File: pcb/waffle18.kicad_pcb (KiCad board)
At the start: 2 copper layers, 39 parts, among them U1 XIAO-RP2350

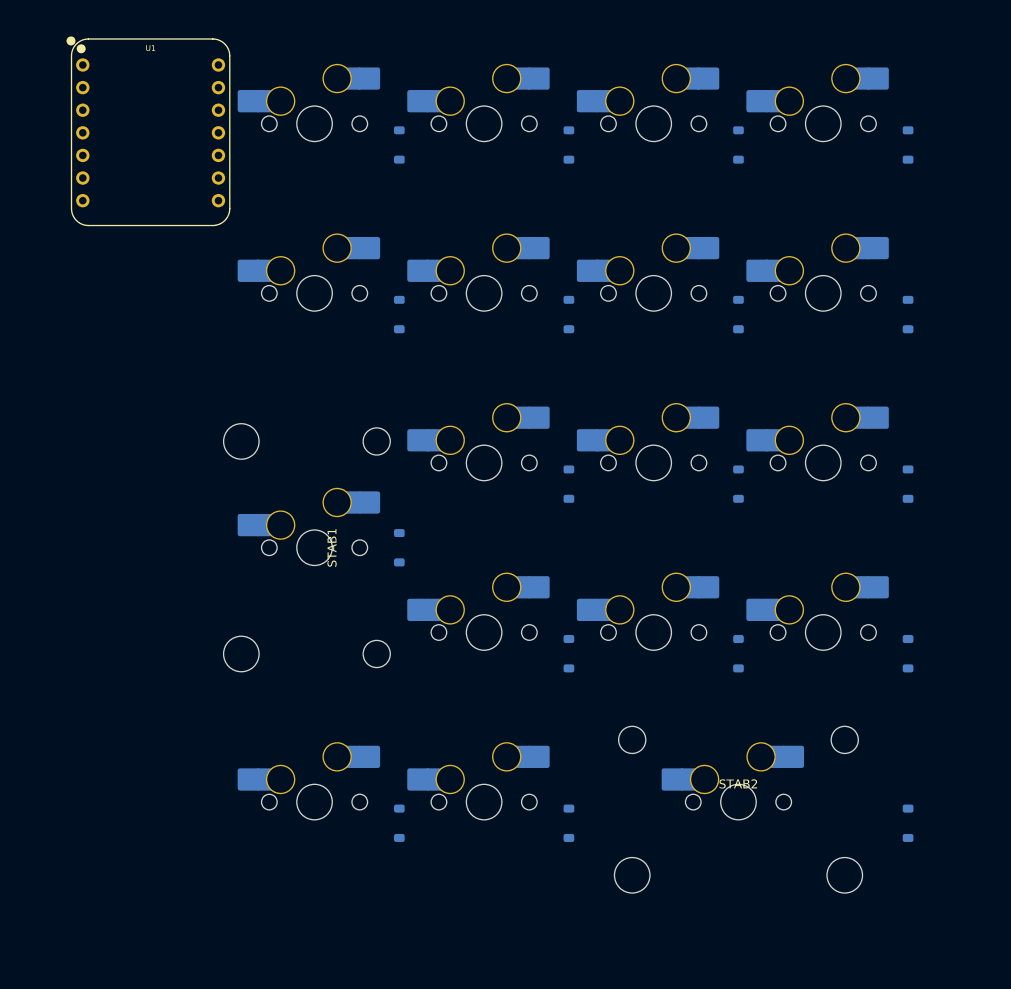
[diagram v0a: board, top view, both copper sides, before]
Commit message: feat(pcb): route tracks and place vias
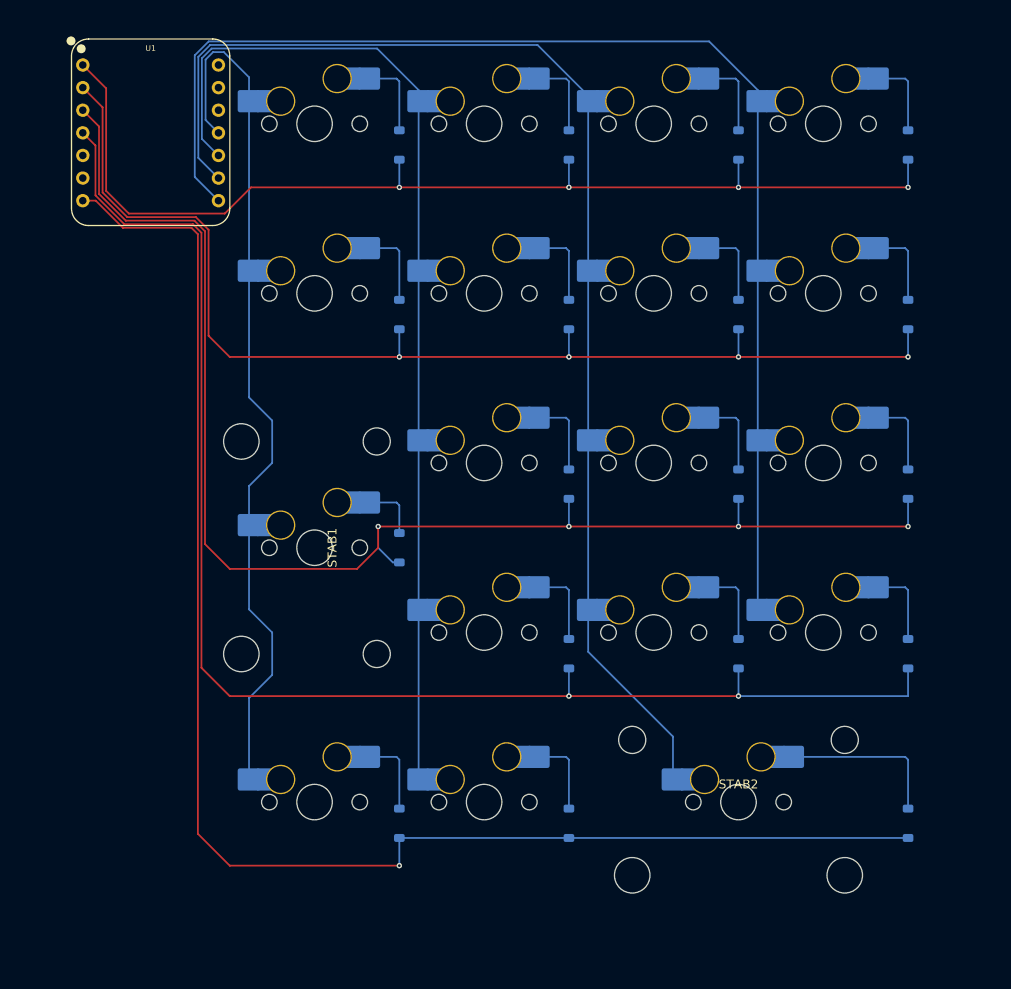
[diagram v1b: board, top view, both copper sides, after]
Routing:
- net /Row 4: track 0.00 -> 166.5 mm, vias 0 -> 1
- net /Row 3: track 0.00 -> 160.2 mm, vias 0 -> 2
- net /Row 2: track 0.00 -> 157.2 mm, vias 0 -> 4
- net /Column 2: track 0.00 -> 142.0 mm
- net /Column 3: track 0.00 -> 142.0 mm
- net /Row 1: track 0.00 -> 130.3 mm, vias 0 -> 4
- net /Row 0: track 0.00 -> 120.0 mm, vias 0 -> 4
- net /Column 1: track 0.00 -> 115.9 mm
- net /Column 0: track 0.00 -> 98.4 mm
- net Net-(D18-A): track 0.00 -> 18.6 mm
- net Net-(D8-A): track 0.00 -> 9.06 mm
- net Net-(D6-A): track 0.00 -> 9.06 mm
- net Net-(D17-A): track 0.00 -> 9.06 mm
- net Net-(D15-A): track 0.00 -> 9.06 mm
- net Net-(D13-A): track 0.00 -> 9.06 mm
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
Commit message: feat(pcb): add edge cuts
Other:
- board outline added: 102.6 x 99.9 mm
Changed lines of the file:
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@@
 		(tags "Cherry MX Keyboard Stabilizer 2.00u 2.25u 2.50u 2.75u Cutout")
 		(property "Reference" "STAB2"
-			(at 0 -2 0)
+			(at 0 9.525 0)
 			(layer "F.SilkS")
 			(effects
@@
 		(tags "Cherry MX Keyboard Stabilizer 2.00u 2.25u 2.50u 2.75u Cutout")
 		(property "Reference" "STAB1"
-			(at 0 -2 90)
+			(at 0 9.525 270)
 			(layer "F.SilkS")
 			(effects
@@
 		(at 96.181074 63.170756 90)
 		(property "Reference" "U1"
-			(at 9.5 0 0)
+			(at 0 -10 90)
 			(unlocked yes)
 			(layer "F.SilkS")
 			(effects
 				(font
-					(size 0.635 0.635)
-					(thickness 0.1016)
+					(size 1 1)
+					(thickness 0.15)
 				)
 			)
@@
 			)
 		)
-		(property "Description" "XIAO-RP2350-SMD by Seeed-Studio/OPL_Kicad_Library on GitHub, used under CC-BY-SA-4.0 / Modified field values"
+		(property "Description" "XIAO-Add-On by Seeed-Studio/OPL_Kicad_Library on GitHub, used under CC-BY-SA-4.0 / Removed unused holes and solderpaste margin overrides"
 			(at 0 0 90)
 			(unlocked yes)
@@
 		(sheetname "/")
 		(sheetfile "waffle18.kicad_sch")
-		(units
-			(unit
-				(name "A")
-				(pins "1" "2" "3" "4" "5" "6" "7" "8" "9" "10" "11" "12" "13" "14" "29"
-					"30" "28" "27" "26" "25" "24" "23" "22" "21" "20" "19" "18" "17" "16"
-					"15"
-				)
-			)
-		)
 		(attr through_hole)
 		(net_tie_pad_groups "1" "2" "3" "4" "5" "6" "7" "8" "9" "10" "11" "12"
@@
 		)
 	)
+	(gr_rect
+		(start 82.291074 51.629756)
+		(end 184.889824 151.498506)
+		(radius 5)
+		(stroke
+			(width 0.05)
+			(type solid)
+		)
+		(fill no)
+		(layer "Edge.Cuts")
+	)
 	(segment

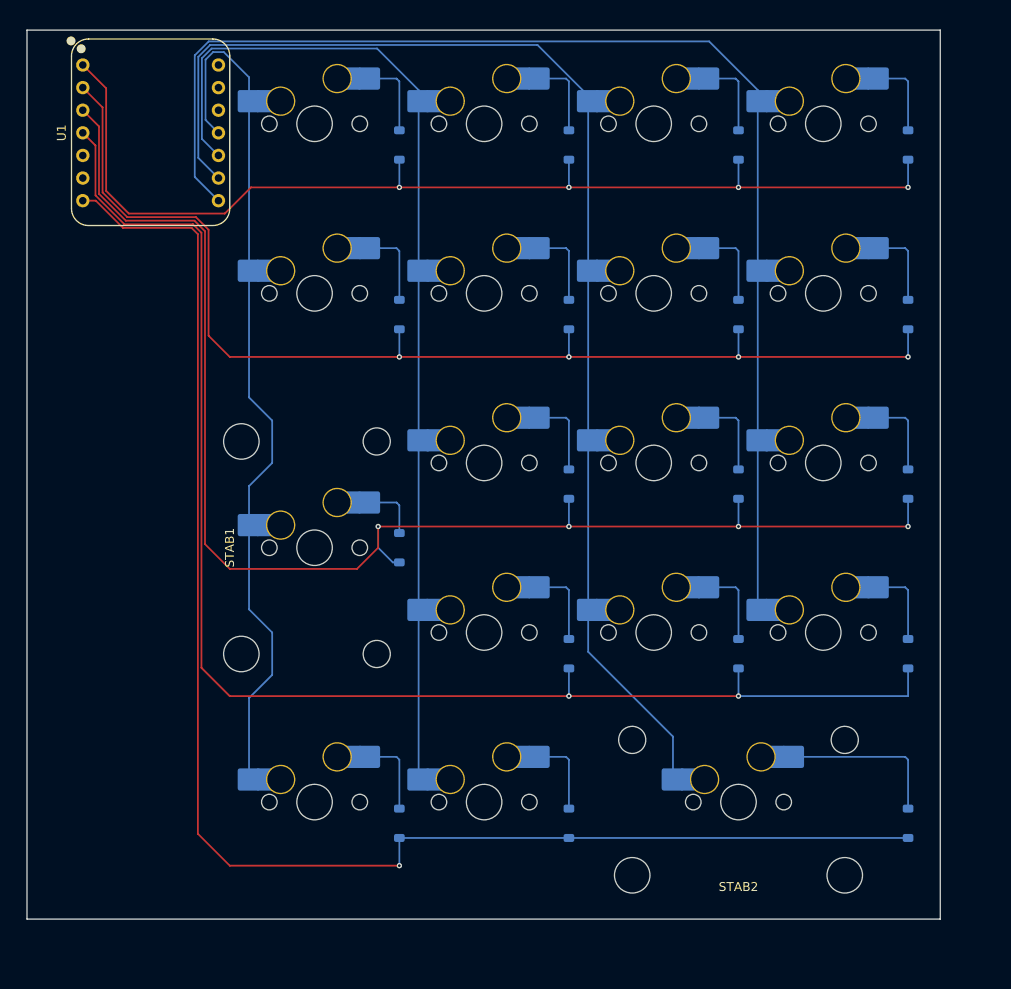
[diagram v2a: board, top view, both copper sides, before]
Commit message: feat(pcb): add mounting holes and filled zone
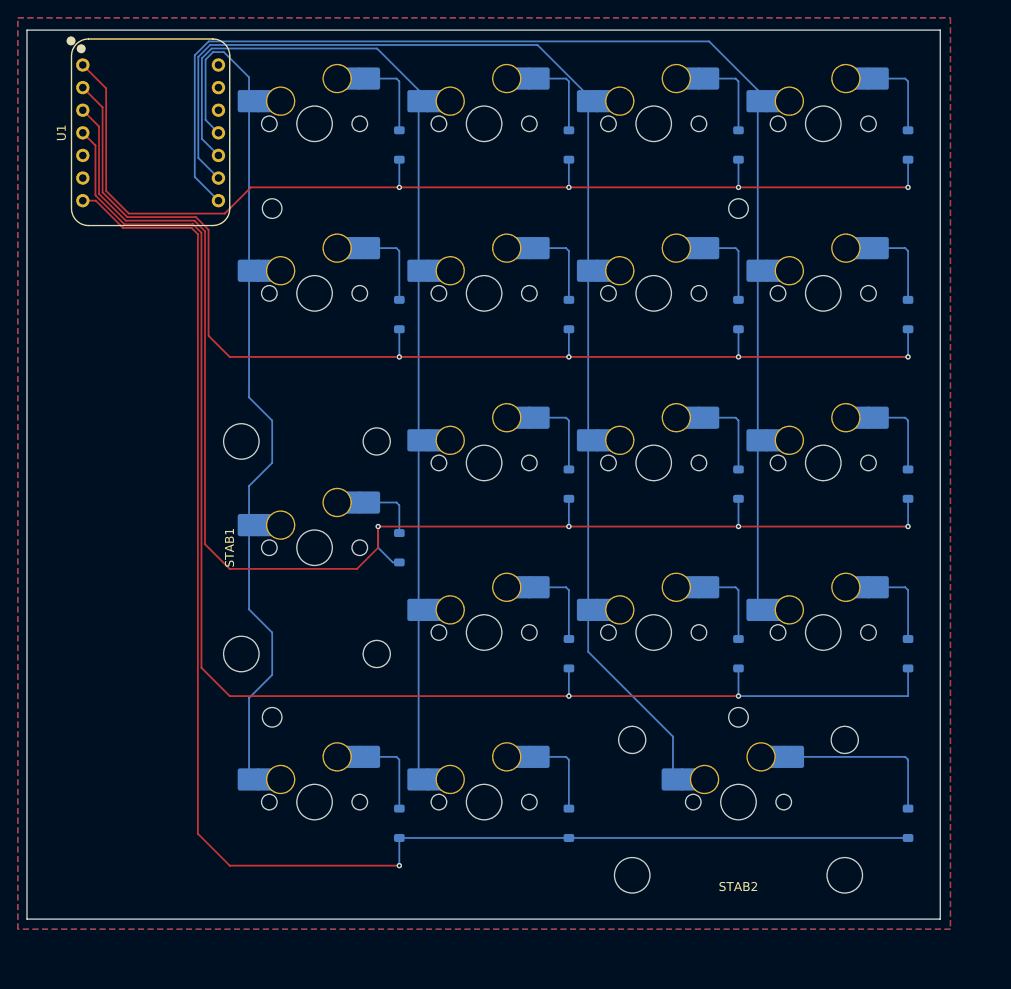
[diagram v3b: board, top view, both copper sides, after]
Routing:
- added copper zone on B.Cu, net (none)
- added copper zone on F.Cu, net (none)
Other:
- outline, holes or cut-outs redrawn
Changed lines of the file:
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@@
+		(layer "Edge.Cuts")
+	)
+	(gr_circle
+		(center 109.833574 71.679756)
+		(end 110.933574 71.679756)
+		(stroke
+			(width 0.05)
+			(type solid)
+		)
+		(fill no)
+		(layer "Edge.Cuts")
+	)
+	(gr_circle
+		(center 109.833574 128.829756)
+		(end 110.933574 128.829756)
+		(stroke
+			(width 0.05)
+			(type solid)
+		)
+		(fill no)
+		(layer "Edge.Cuts")
+	)
+	(gr_circle
+		(center 162.221074 71.679756)
+		(end 163.321074 71.679756)
+		(stroke
+			(width 0.05)
+			(type solid)
+		)
+		(fill no)
+		(layer "Edge.Cuts")
+	)
+	(gr_circle
+		(center 162.221074 128.829756)
+		(end 163.321074 128.829756)
+		(stroke
+			(width 0.05)
+			(type solid)
+		)
+		(fill no)
 		(layer "Edge.Cuts")
 	)
@@
 		(net "Net-(D2-A)")
 	)
+	(zone
+		(layers "F.Cu" "B.Cu")
+		(hatch edge 0.5)
+		(connect_pads
+			(clearance 0.3)
+		)
+		(min_thickness 0.25)
+		(fill yes
+			(thermal_gap 0.5)
+			(thermal_bridge_width 0.5)
+			(island_removal_mode 1)
+		)
+		(polygon
+			(pts
+				(xy 81.258574 50.248506) (xy 186.033574 50.248506) (xy 186.033574 152.642256) (xy 81.258574 152.642256)
+			)
+		)
+	)
 	(embedded_fonts no)

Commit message: chore(pcb): prepare for production
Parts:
- moved D1 6.74 mm to (128.9, 69.3)
- moved D11 6.74 mm to (167.0, 107.4)
- moved D3 6.74 mm to (167.0, 69.3)
- moved D5 6.74 mm to (128.9, 88.3)
- moved D7 6.74 mm to (167.0, 88.3)
- moved S12 6.74 mm to (176.5, 105.0)
- moved S15 6.74 mm to (176.5, 124.1)
- moved S8 6.74 mm to (176.5, 86.0)
- moved S4 6.74 mm to (176.5, 66.9)
- moved S5 6.74 mm to (119.4, 86.0)
- moved U1 6.74 mm to (100.9, 67.9)
- moved D14 6.74 mm to (167.0, 126.4)
- moved D16 6.74 mm to (128.9, 145.5)
- moved D9 6.74 mm to (128.9, 114.5)
- moved S18 6.74 mm to (167.0, 143.1)
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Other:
- outline, holes or cut-outs redrawn
- board text added: "waffle18 Rev 0.1 Designed by glAx"
